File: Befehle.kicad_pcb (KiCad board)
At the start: 2 copper layers, 100 x 160 mm, 36 parts, among them P1 CONN_01X07, P2 CONN_02X10, U2 74LS04, U3 7400, U5 74LS541, U6 74LS373, U7 74LS139, U8 74LS540

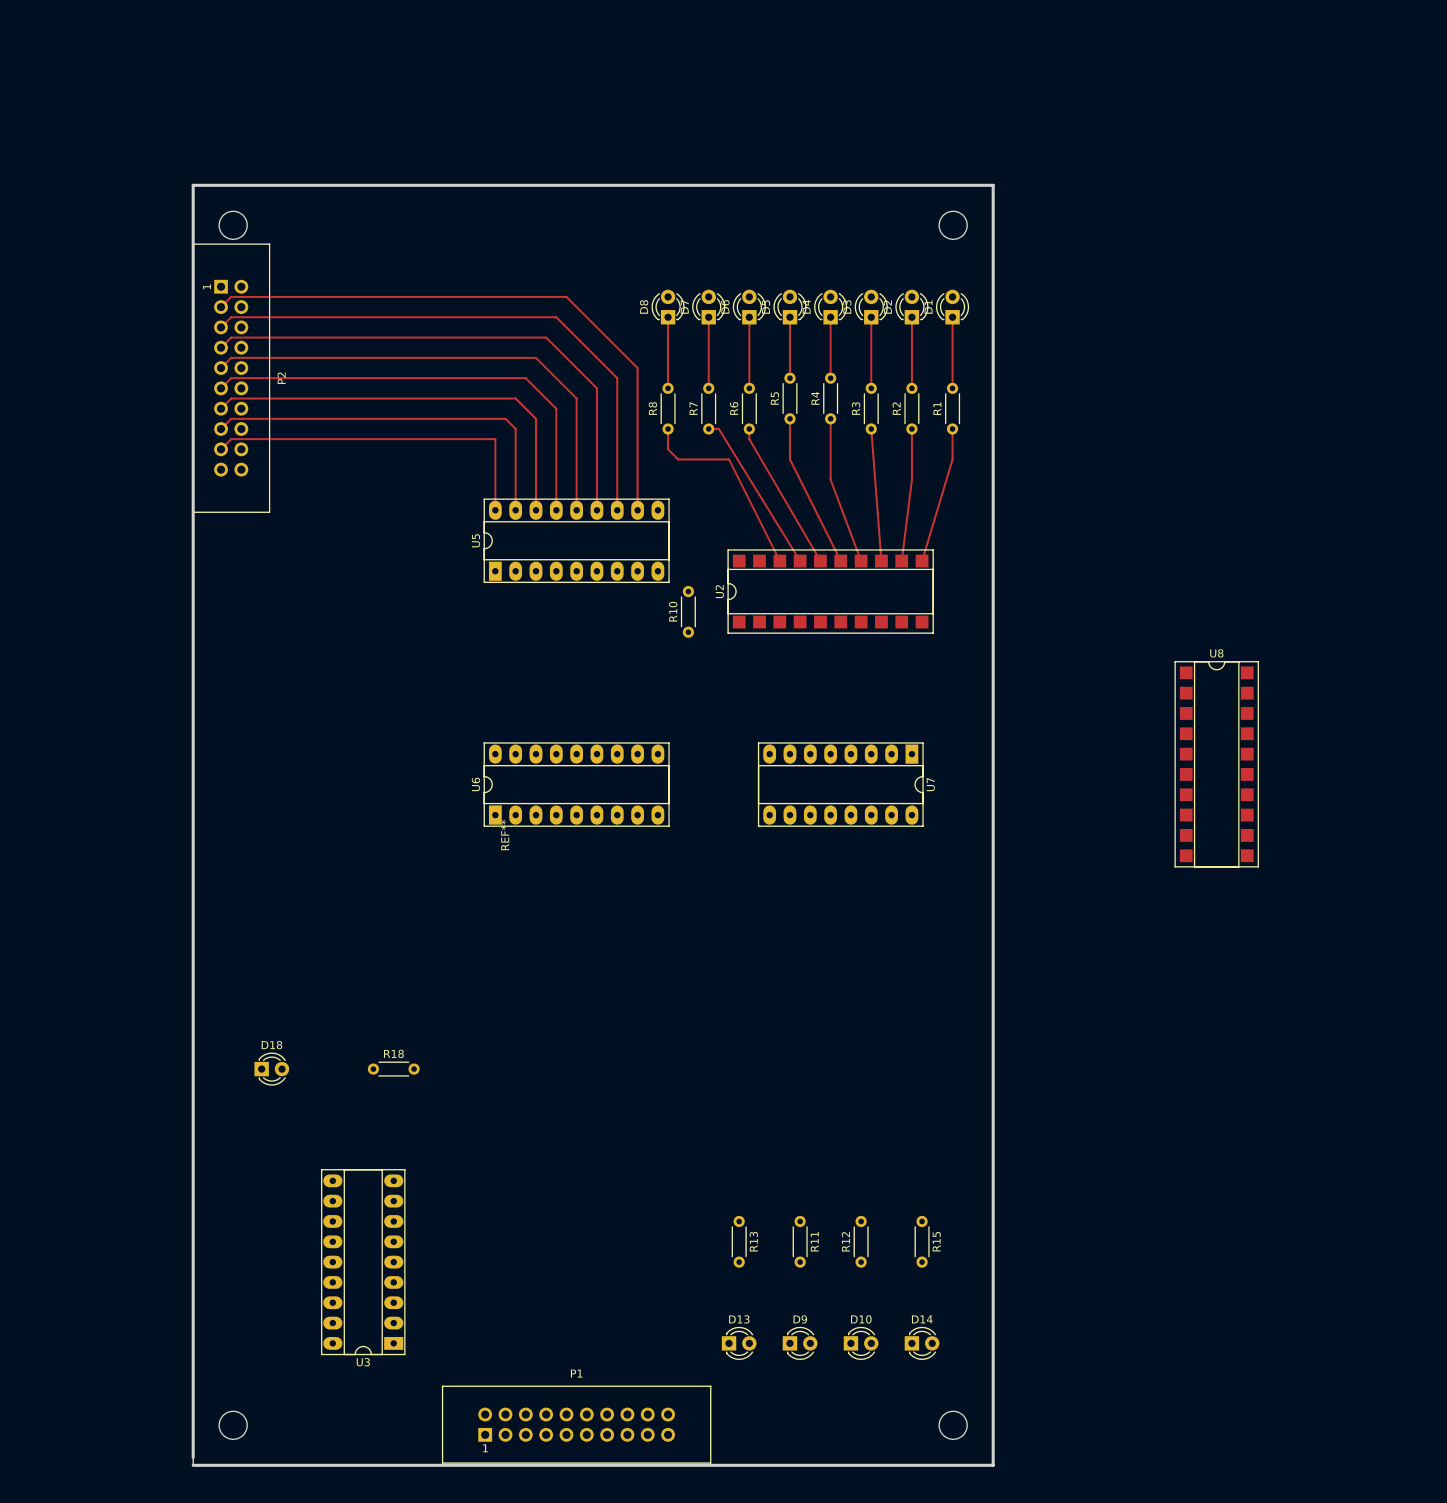
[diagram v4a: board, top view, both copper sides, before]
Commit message: Footprints added
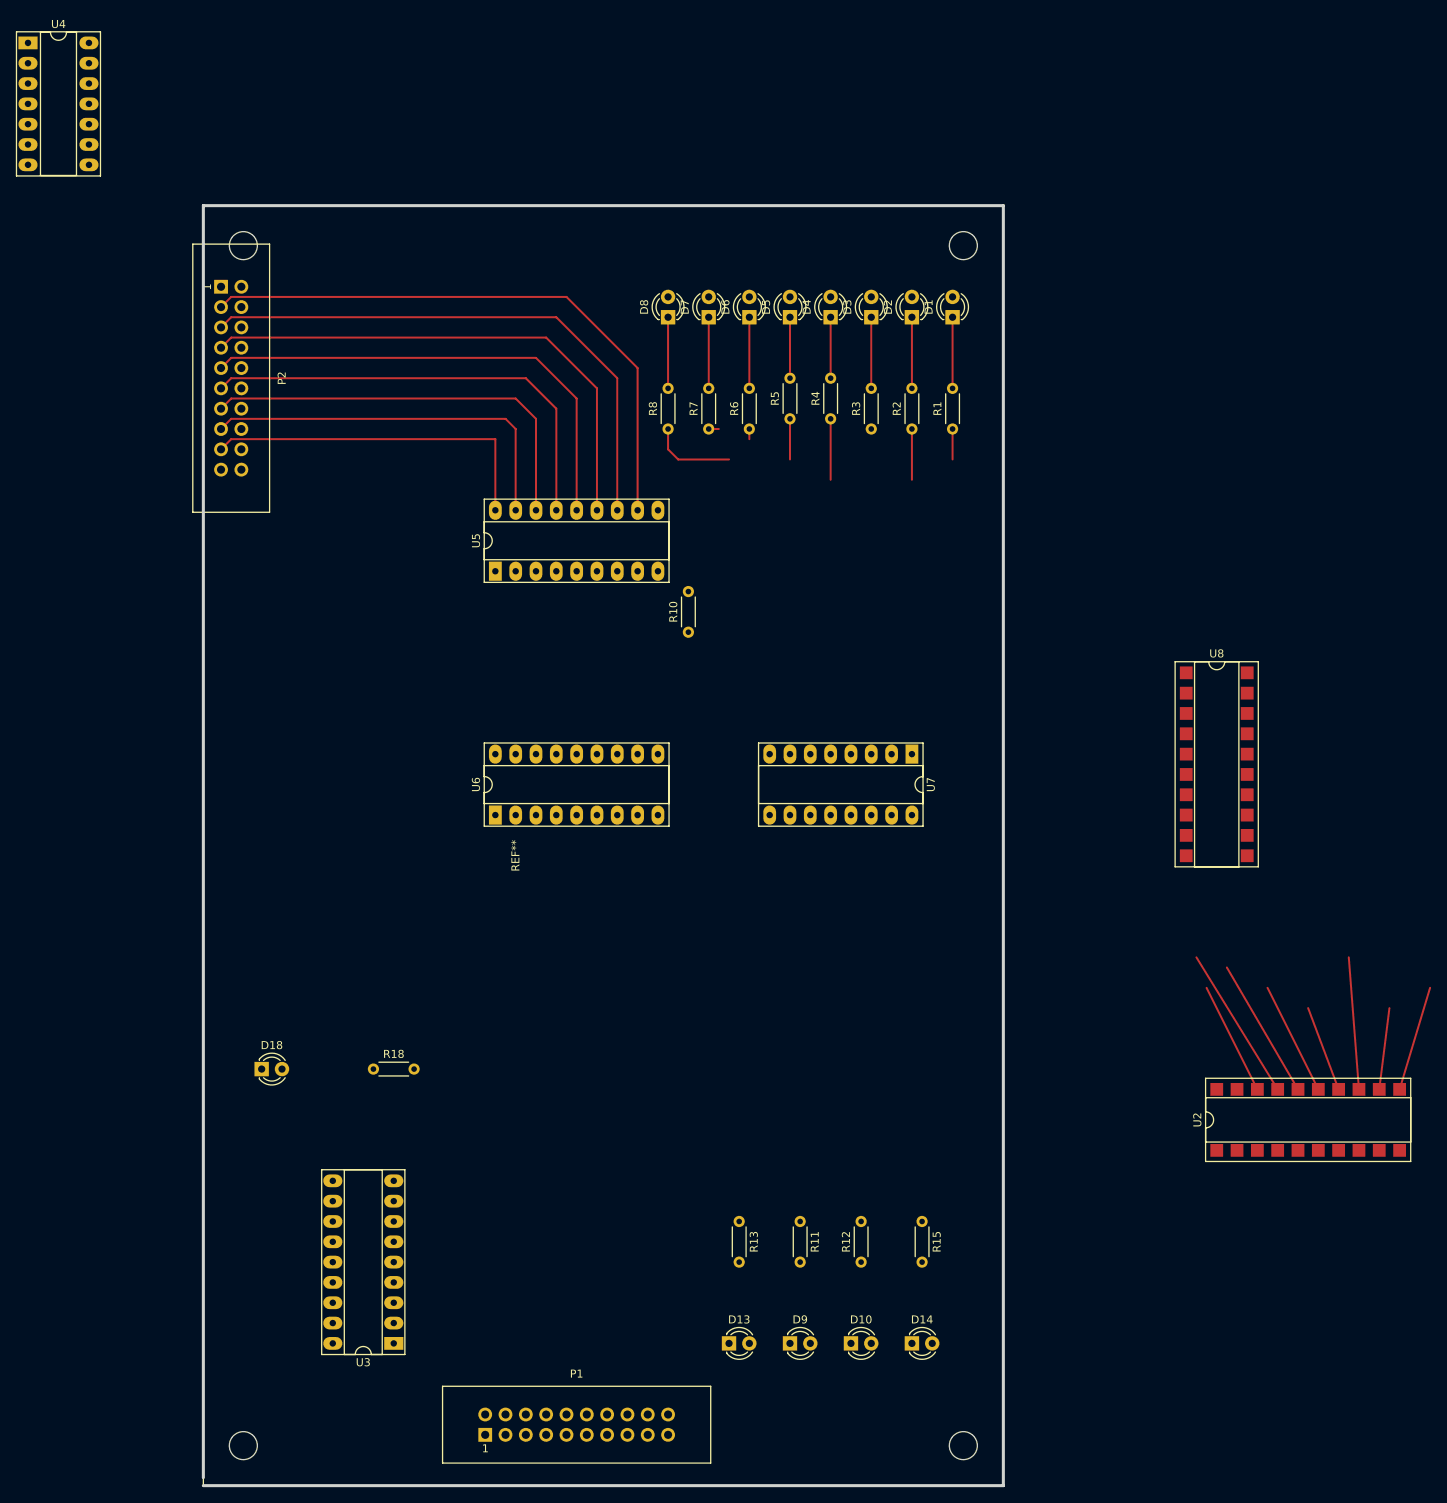
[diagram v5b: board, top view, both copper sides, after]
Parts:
- added U4: 74HCT02, Housings_DIP:DIP-14_W7.62mm_Socket_LongPads, F.Cu at (0.00, 0.00)
- P1: value CONN_01X07 -> CONN_02X10
- moved U2 89.0 mm to (160.0, 134.6)
- moved REF** 2.84 mm to (121.9, 180.3)
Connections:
- net Net-(U6-Pad3) renamed /d8
- P1 pad 10: (no net) -> Net-(P1-Pad10)
- P1 pad 11: (no net) -> Net-(P1-Pad11)
- P1 pad 12: (no net) -> Net-(P1-Pad12)
- P1 pad 13: (no net) -> Net-(P1-Pad13)
- P1 pad 14: (no net) -> Net-(P1-Pad14)
- P1 pad 15: (no net) -> Net-(P1-Pad15)
- P1 pad 16: (no net) -> Net-(P1-Pad16)
- P1 pad 17: (no net) -> Net-(P1-Pad17)
- P1 pad 18: (no net) -> Net-(P1-Pad18)
- P1 pad 19: (no net) -> Net-(P1-Pad19)
- P1 pad 20: (no net) -> Net-(P1-Pad20)
- P1 pad 8: (no net) -> Net-(P1-Pad8)
- P1 pad 9: (no net) -> Net-(P1-Pad9)
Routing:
- net (no net): track 0.00 -> 65.4 mm
- net Net-(R7-Pad1): track 20.7 -> 1.27 mm
- net Net-(D4-Pad1): track 26.5 -> 8.89 mm
- net 0: track 0.00 -> 16.6 mm
- net Net-(D2-Pad1): track 25.4 -> 8.89 mm
- net Net-(R8-Pad1): track 24.9 -> 10.7 mm
- net Net-(R5-Pad1): track 19.3 -> 5.08 mm

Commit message: footprints added
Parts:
- removed D2: Led_Small, LEDs:LED_D3.0mm
- removed D3: LED, LEDs:LED_D3.0mm
- U2: value 74LS04 -> 74540; footprint Housings_DIP:DIP-20_W7.62mm_SMDSocket_SmallPads -> Housings_DIP:DIP-18_W7.62mm_Socket_LongPads
- U3: footprint Housings_DIP:DIP-18_W7.62mm_Socket_LongPads -> Housings_DIP:DIP-14_W7.62mm_Socket_LongPads
- U5, U6: footprint Housings_DIP:DIP-18_W7.62mm_Socket_LongPads -> Housings_DIP:DIP-20_W7.62mm_Socket_LongPads
- U8: footprint Housings_DIP:DIP-20_W7.62mm_SMDSocket_SmallPads -> Housings_DIP:DIP-20_W7.62mm_Socket_LongPads
- moved U4 100.8 mm to (33.0, 95.2)
- moved U2 68.6 mm to (91.4, 134.6)
- moved U8 60.9 mm to (92.7, 66.0), turned to 90 degrees
- moved D18 30.6 mm to (26.7, 97.8), turned to 90 degrees
- moved R18 26.2 mm to (26.7, 108.0), turned to 90 degrees
- moved U3 21.1 mm to (34.3, 144.8), turned to 0 degrees
- moved U7 18.2 mm to (94.0, 96.5), turned to 90 degrees
- moved R12 5.08 mm to (104.1, 147.3), turned to 270 degrees
- moved U5 2.84 mm to (55.9, 67.3)
- moved D14 1.80 mm to (111.8, 161.3), turned to 270 degrees
- moved D10 1.80 mm to (104.1, 161.3), turned to 270 degrees
- moved D9 1.80 mm to (96.5, 161.3), turned to 270 degrees
- moved D13 1.27 mm to (87.6, 161.3), turned to 270 degrees
- moved R13 1.27 mm to (87.6, 147.3)
- moved U6 1.27 mm to (57.1, 96.5)
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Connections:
- D5 pad 2: Net-(D5-Pad2) -> VCC
- U2 pad 1: Net-(R4-Pad1) -> Net-(U2-Pad1)
- U2 pad 10: Net-(R17-Pad2) -> GND
- U2 pad 11: 1 -> (no net)
- U2 pad 12: Net-(R21-Pad2) -> (no net)
- U2 pad 13: 0 -> (no net)
- U2 pad 14: VCC -> (no net)
- U2 pad 18: (no net) -> Net-(R2-Pad2)
- U2 pad 2: Net-(R2-Pad2) -> Net-(R4-Pad1)
- U2 pad 3: loadIR -> (no net)
- U2 pad 4: Net-(R5-Pad2) -> (no net)
- U2 pad 5: 3 -> (no net)
- U2 pad 6: Net-(R6-Pad2) -> (no net)
- U2 pad 7: GND -> (no net)
- U2 pad 8: Net-(R9-Pad2) -> (no net)
- U2 pad 9: 2 -> (no net)
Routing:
- net Net-(P2-Pad7): track 65.4 -> 1.80 mm
- net Net-(P2-Pad9): track 61.1 -> 1.80 mm
- net Net-(P2-Pad11): track 56.7 -> 1.80 mm
- net Net-(P2-Pad13): track 52.4 -> 1.80 mm
- net Net-(P2-Pad15): track 48.0 -> 1.80 mm
- net Net-(P2-Pad17): track 43.7 -> 1.80 mm
- net (no net): track 65.4 -> 41.9 mm
- net 0: track 16.6 -> 0.00 mm
- net 1: track 13.3 -> 0.00 mm
- net VCC: track 14.7 -> 3.81 mm
- net Net-(R21-Pad2): track 10.2 -> 0.00 mm
- net Net-(R3-Pad2): track 0.00 -> 8.89 mm
- net Net-(R2-Pad2): track 0.00 -> 8.89 mm
- net Net-(D3-Pad1): track 8.89 -> 0.00 mm
- net Net-(D2-Pad1): track 8.89 -> 0.00 mm
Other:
- board size 100 x 160 mm -> 160 x 100 mm

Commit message: beschriftungen organisiert
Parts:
- added U1: 74LS14, Housings_DIP:DIP-14_W7.62mm_Socket_LongPads, F.Cu at (33.0, 69.8)
- moved R18 107.8 mm to (115.6, 47.0)
- moved D18 105.2 mm to (110.5, 34.3)
- moved R1 93.0 mm to (25.4, 71.1)
- moved REF** 3.59 mm to (119.4, 177.8), turned to 90 degrees
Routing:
- net enableR: track 0.00 -> 95.6 mm
- net VCC: track 3.81 -> 92.2 mm
- net Net-(R2-Pad2): track 8.89 -> 0.00 mm
- net Net-(D18-Pad1): track 0.00 -> 8.89 mm
- net Net-(D1-Pad1): track 15.2 -> 6.35 mm
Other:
- board size 160 x 100 mm -> 100 x 160 mm
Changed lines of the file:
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@@
 (kicad_pcb (version 4) (host pcbnew 4.0.4+e1-6308~48~ubuntu16.04.1-stable)
   (general
-    (links 75)
-    (no_connects 75)
+    (links 82)
+    (no_connects 82)
     (area 0 0 0 0)
     (thickness 1.6)
@@
     (tracks 34)
     (zones 0)
-    (modules 35)
-    (nets 117)
+    (modules 36)
+    (nets 118)
   )
   (page A4)
@@
   (net 115 /d8)
   (net 116 "Net-(U2-Pad1)")
+  (net 117 "Net-(U1-Pad2)")
   (net_class Default "This is the default net class."
     (clearance 0.2)
@@
     (add_net "Net-(R7-Pad1)")
     (add_net "Net-(R8-Pad1)")
+    (add_net "Net-(U1-Pad2)")
     (add_net "Net-(U1-Pad6)")
     (add_net "Net-(U2-Pad1)")
@@
   )
   (module EuroBoard_Outline:EuroBoard160mmX100mm_holes (layer F.Cu)
-    (at 121.92 180.34 180)
+    (at 119.38 177.8 90)
     (descr "Outline, Eurocard, 100x160mm, with holes 3,5mm,")
     (tags "Outline, Eurocard, 100x160mm, with holes 3,5mm,")
-    (fp_text reference REF** (at 78.74 -60.96 180) (layer F.SilkS)
-      (effects (font (size 1 1) (thickness 0.15)))
-    )
-    (fp_text value EuroBoard160mmX100mm_holes (at 85.09 -35.56 180) (layer F.Fab)
+    (fp_text reference REF** (at 78.74 -60.96 90) (layer F.SilkS)
+      (effects (font (size 1 1) (thickness 0.15)))
+    )
+    (fp_text value EuroBoard160mmX100mm_holes (at 85.09 -35.56 90) (layer F.Fab)
       (effects (font (size 1 1) (thickness 0.15)))
     )
@@
     (fp_line (start 159.99968 0) (end 159.99968 -99.9998) (layer Edge.Cuts) (width 0.381))
     (fp_line (start 159.99968 -99.9998) (end 1.00076 -99.9998) (layer Edge.Cuts) (width 0.381))
-    (pad "" np_thru_hole circle (at 5.00126 -95.00108 180) (size 3.50012 3.50012) (drill 3.50012) (layers *.Cu *.Mask))
-    (pad "" np_thru_hole circle (at 155.00096 -95.00108 180) (size 3.50012 3.50012) (drill 3.50012) (layers *.Cu *.Mask))
-    (pad "" np_thru_hole circle (at 155.00096 -5.00126 180) (size 3.50012 3.50012) (drill 3.50012) (layers *.Cu *.Mask))
-    (pad "" np_thru_hole circle (at 5.00126 -5.00126 180) (size 3.50012 3.50012) (drill 3.50012) (layers *.Cu *.Mask))
+    (pad "" np_thru_hole circle (at 5.00126 -95.00108 90) (size 3.50012 3.50012) (drill 3.50012) (layers *.Cu *.Mask))
+    (pad "" np_thru_hole circle (at 155.00096 -95.00108 90) (size 3.50012 3.50012) (drill 3.50012) (layers *.Cu *.Mask))
+    (pad "" np_thru_hole circle (at 155.00096 -5.00126 90) (size 3.50012 3.50012) (drill 3.50012) (layers *.Cu *.Mask))
+    (pad "" np_thru_hole circle (at 5.00126 -5.00126 90) (size 3.50012 3.50012) (drill 3.50012) (layers *.Cu *.Mask))
   )
   (module Resistors_ThroughHole:R_Axial_DIN0204_L3.6mm_D1.6mm_P5.08mm_Horizontal (layer F.Cu)
-    (at 115.57 48.26 90)
+    (at 25.4 71.12 90)
     (descr "Resistor, Axial_DIN0204 series, Axial, Horizontal, pin pitch=5.08mm, 0.16666666666666666W = 1/6W, length*diameter=3.6*1.6mm^2, http://cdn-reichelt.de/documents/datenblatt/B400/1_4W%23YAG.pdf")
     (tags "Resistor Axial_DIN0204 series Axial Horizontal pin pitch 5.08mm 0.16666666666666666W = 1/6W length 3.6mm diameter 1.6mm")
@@
   )
   (module LEDs:LED_D3.0mm (layer F.Cu)
-    (at 26.67 97.79 90)
+    (at 110.49 34.29 90)
     (descr "LED, diameter 3.0mm, 2 pins")
     (tags "LED diameter 3.0mm 2 pins")
@@
   )
   (module Resistors_ThroughHole:R_Axial_DIN0204_L3.6mm_D1.6mm_P5.08mm_Horizontal (layer F.Cu)
-    (at 26.67 107.95 90)
+    (at 115.57 46.99 90)
     (descr "Resistor, Axial_DIN0204 series, Axial, Horizontal, pin pitch=5.08mm, 0.16666666666666666W = 1/6W, length*diameter=3.6*1.6mm^2, http://cdn-reichelt.de/documents/datenblatt/B400/1_4W%23YAG.pdf")
     (tags "Resistor Axial_DIN0204 series Axial Horizontal pin pitch 5.08mm 0.16666666666666666W = 1/6W length 3.6mm diameter 1.6mm")
@@
     )
   )
+  (module Housings_DIP:DIP-14_W7.62mm_Socket_LongPads (layer F.Cu)
+    (at 33.02 69.85)
+    (descr "14-lead though-hole mounted DIP package, row spacing 7.62 mm (300 mils), Socket, LongPads")
+    (tags "THT DIP DIL PDIP 2.54mm 7.62mm 300mil Socket LongPads")
+    (fp_text reference U1 (at 3.81 -2.33) (layer F.SilkS)
+      (effects (font (size 1 1) (thickness 0.15)))
+    )
+    (fp_text value 74LS14 (at 3.81 17.57) (layer F.Fab)
+      (effects (font (size 1 1) (thickness 0.15)))
+    )
+    (fp_arc (start 3.81 -1.33) (end 2.81 -1.33) (angle -180) (layer F.SilkS) (width 0.12))
+    (fp_line (start 1.635 -1.27) (end 6.985 -1.27) (layer F.Fab) (width 0.1))
+    (fp_line (start 6.985 -1.27) (end 6.985 16.51) (layer F.Fab) (width 0.1))
+    (fp_line (start 6.985 16.51) (end 0.635 16.51) (layer F.Fab) (width 0.1))
+    (fp_line (start 0.635 16.51) (end 0.635 -0.27) (layer F.Fab) (width 0.1))
+    (fp_line (start 0.635 -0.27) (end 1.635 -1.27) (layer F.Fab) (width 0.1))
+    (fp_line (start -1.27 -1.33) (end -1.27 16.57) (layer F.Fab) (width 0.1))
+    (fp_line (start -1.27 16.57) (end 8.89 16.57) (layer F.Fab) (width 0.1))
+    (fp_line (start 8.89 16.57) (end 8.89 -1.33) (layer F.Fab) (width 0.1))
+    (fp_line (start 8.89 -1.33) (end -1.27 -1.33) (layer F.Fab) (width 0.1))
+    (fp_line (start 2.81 -1.33) (end 1.56 -1.33) (layer F.SilkS) (width 0.12))
+    (fp_line (start 1.56 -1.33) (end 1.56 16.57) (layer F.SilkS) (width 0.12))
+    (fp_line (start 1.56 16.57) (end 6.06 16.57) (layer F.SilkS) (width 0.12))
+    (fp_line (start 6.06 16.57) (end 6.06 -1.33) (layer F.SilkS) (width 0.12))
+    (fp_line (start 6.06 -1.33) (end 4.81 -1.33) (layer F.SilkS) (width 0.12))
+    (fp_line (start -1.44 -1.39) (end -1.44 16.63) (layer F.SilkS) (width 0.12))
+    (fp_line (start -1.44 16.63) (end 9.06 16.63) (layer F.SilkS) (width 0.12))
+    (fp_line (start 9.06 16.63) (end 9.06 -1.39) (layer F.SilkS) (width 0.12))
+    (fp_line (start 9.06 -1.39) (end -1.44 -1.39) (layer F.SilkS) (width 0.12))
+    (fp_line (start -1.55 -1.6) (end -1.55 16.85) (layer F.CrtYd) (width 0.05))
+    (fp_line (start -1.55 16.85) (end 9.15 16.85) (layer F.CrtYd) (width 0.05))
+    (fp_line (start 9.15 16.85) (end 9.15 -1.6) (layer F.CrtYd) (width 0.05))
+    (fp_line (start 9.15 -1.6) (end -1.55 -1.6) (layer F.CrtYd) (width 0.05))
+    (fp_text user %R (at 3.81 7.62) (layer F.Fab)
+      (effects (font (size 1 1) (thickness 0.15)))
+    )
+    (pad 1 thru_hole rect (at 0 0) (size 2.4 1.6) (drill 0.8) (layers *.Cu *.Mask)
+      (net 62 enableR))
+    (pad 8 thru_hole oval (at 7.62 15.24) (size 2.4 1.6) (drill 0.8) (layers *.Cu *.Mask))
+    (pad 2 thru_hole oval (at 0 2.54) (size 2.4 1.6) (drill 0.8) (layers *.Cu *.Mask)
+      (net 117 "Net-(U1-Pad2)"))
+    (pad 9 thru_hole oval (at 7.62 12.7) (size 2.4 1.6) (drill 0.8) (layers *.Cu *.Mask))
+    (pad 3 thru_hole oval (at 0 5.08) (size 2.4 1.6) (drill 0.8) (layers *.Cu *.Mask)
+      (net 117 "Net-(U1-Pad2)"))
+    (pad 10 thru_hole oval (at 7.62 10.16) (size 2.4 1.6) (drill 0.8) (layers *.Cu *.Mask))
+    (pad 4 thru_hole oval (at 0 7.62) (size 2.4 1.6) (drill 0.8) (layers *.Cu *.Mask)
+      (net 64 "Net-(R3-Pad2)"))
+    (pad 11 thru_hole oval (at 7.62 7.62) (size 2.4 1.6) (drill 0.8) (layers *.Cu *.Mask))
+    (pad 5 thru_hole oval (at 0 10.16) (size 2.4 1.6) (drill 0.8) (layers *.Cu *.Mask)
+      (net 117 "Net-(U1-Pad2)"))
+    (pad 12 thru_hole oval (at 7.62 5.08) (size 2.4 1.6) (drill 0.8) (layers *.Cu *.Mask))
+    (pad 6 thru_hole oval (at 0 12.7) (size 2.4 1.6) (drill 0.8) (layers *.Cu *.Mask)
+      (net 78 "Net-(U1-Pad6)"))
+    (pad 13 thru_hole oval (at 7.62 2.54) (size 2.4 1.6) (drill 0.8) (layers *.Cu *.Mask))
+    (pad 7 thru_hole oval (at 0 15.24) (size 2.4 1.6) (drill 0.8) (layers *.Cu *.Mask)
+      (net 27 GND))
+    (pad 14 thru_hole oval (at 7.62 0) (size 2.4 1.6) (drill 0.8) (layers *.Cu *.Mask)
+      (net 28 VCC))
+    (model ${KISYS3DMOD}/Housings_DIP.3dshapes/DIP-14_W7.62mm_Socket.wrl
+      (at (xyz 0 0 0))
+      (scale (xyz 1 1 1))
+      (rotate (xyz 0 0 0))
+    )
+  )
   (segment (start 66.04 58.42) (end 66.04 45.72) (width 0.25) (layer F.Cu) (net 0) (status 10))
   (segment (start 71.12 58.42) (end 71.12 43.18) (width 0.25) (layer F.Cu) (net 0) (status 10))
@@
   (segment (start 81.28 52.07) (end 87.63 52.07) (width 0.25) (layer F.Cu) (net 25))
   (segment (start 80.01 50.8) (end 81.28 52.07) (width 0.25) (layer F.Cu) (net 25))
-  (segment (start 115.57 48.26) (end 115.57 52.07) (width 0.25) (layer F.Cu) (net 28) (status 10))
+  (segment (start 25.4 71.12) (end 115.57 52.07) (width 0.25) (layer F.Cu) (net 28) (status 10))
   (segment (start 110.49 48.26) (end 110.49 54.61) (width 0.25) (layer F.Cu) (net 30))
-  (segment (start 115.57 34.29) (end 115.57 43.18) (width 0.25) (layer F.Cu) (net 30) (status 20))
   (segment (start 90.17 48.26) (end 90.17 49.53) (width 0.25) (layer F.Cu) (net 32))
   (segment (start 100.33 34.29) (end 100.33 41.91) (width 0.25) (layer F.Cu) (net 32) (status 20))
@@
   (segment (start 85.09 34.29) (end 85.09 43.18) (width 0.25) (layer F.Cu) (net 35))
   (segment (start 80.01 34.29) (end 80.01 43.18) (width 0.25) (layer F.Cu) (net 36))
+  (segment (start 110.49 34.29) (end 110.49 43.18) (width 0.25) (layer F.Cu) (net 47))
   (segment (start 25.4 39.37) (end 24.13 40.64) (width 0.25) (layer F.Cu) (net 50))
   (segment (start 25.4 41.91) (end 24.13 43.18) (width 0.25) (layer F.Cu) (net 52))
@@
   (segment (start 25.4 46.99) (end 24.13 48.26) (width 0.25) (layer F.Cu) (net 56))
   (segment (start 25.4 49.53) (end 24.13 50.8) (width 0.25) (layer F.Cu) (net 58))
-  (segment (start 110.49 34.29) (end 110.49 43.18) (width 0.25) (layer F.Cu) (net 63))
+  (segment (start 115.57 34.29) (end 25.4 66.04) (width 0.25) (layer F.Cu) (net 62) (status 20))
   (segment (start 105.41 34.29) (end 105.41 43.18) (width 0.25) (layer F.Cu) (net 64))
 )
